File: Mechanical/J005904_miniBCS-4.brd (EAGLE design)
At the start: 146.1 x 146.1 mm, 173 parts, among them IC1 WIZ850io, J11 QWIIC_RIGHT_ANGLE, J14 A0/A1, J2 1734035-2, M2 TEENSY4.1, U1 ADA4084, U10 MAX11300GCM, U11 CAT811, U2 2G17, U3 ISL23425, U4 AD9833, U5 ISO1H815G, U6 78L12, U7 ADM3312/5, U8 2G17, U9 79L12, X1 OSC-OE-CFPS-9

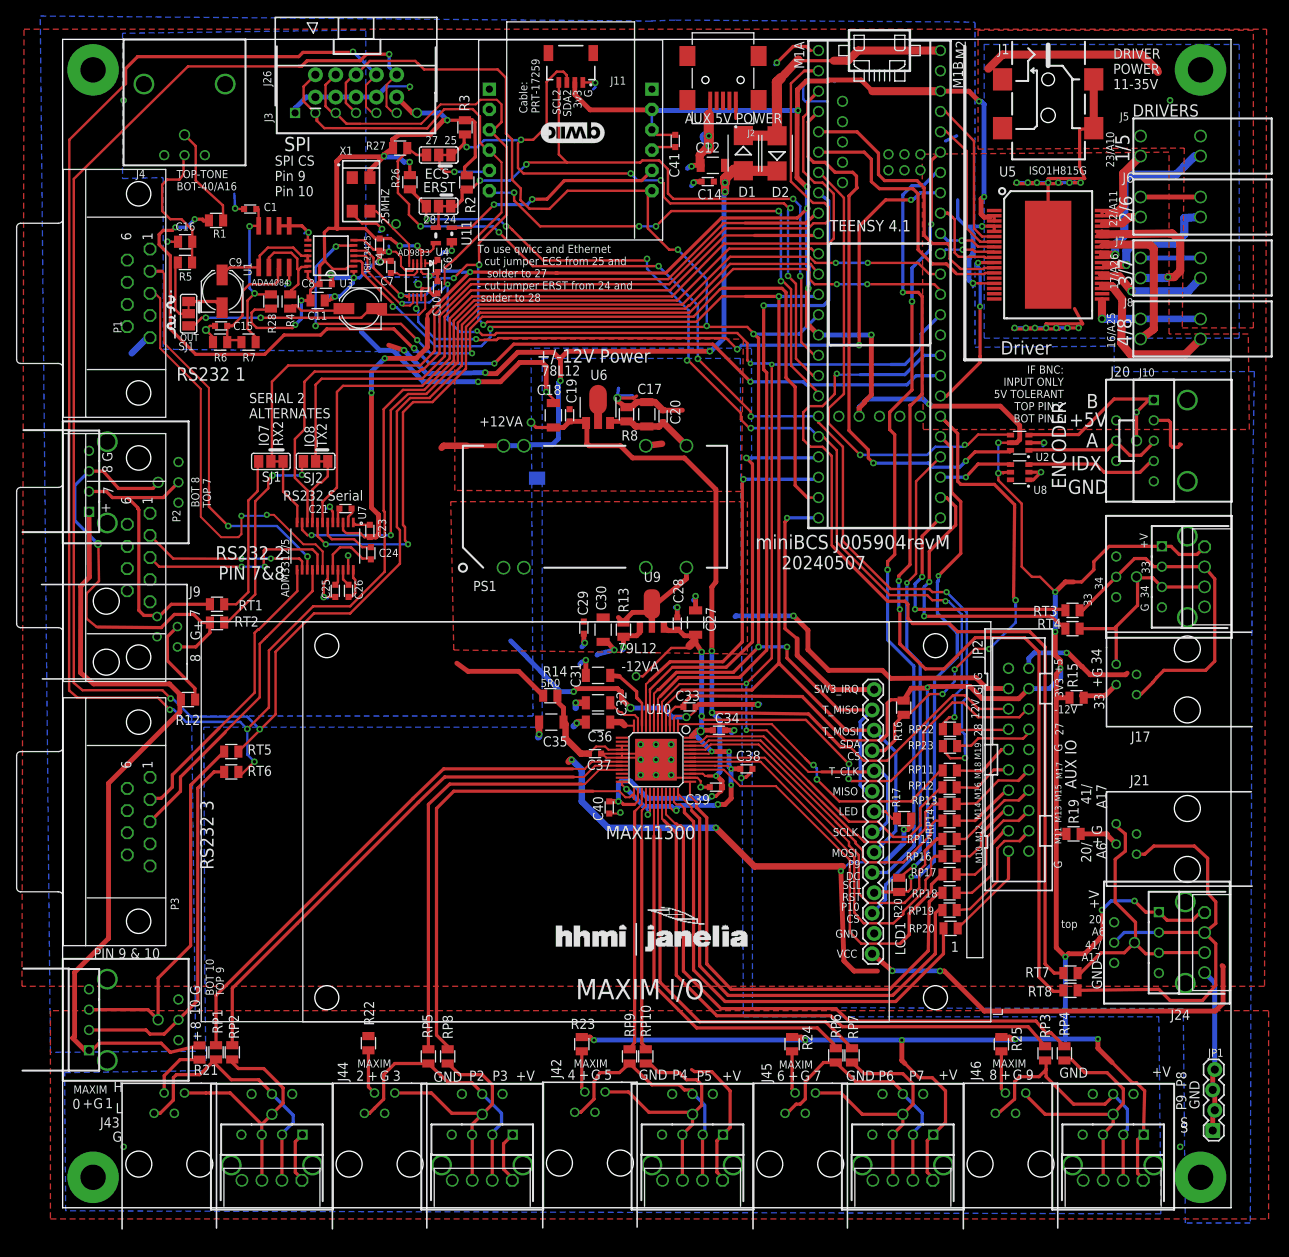
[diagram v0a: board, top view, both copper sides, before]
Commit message: Add SPI and I2C connectors
Add external connections for SPI with two chip selects on 10 pin ribbon or 7 pin header
Add QWIIC I2C connection
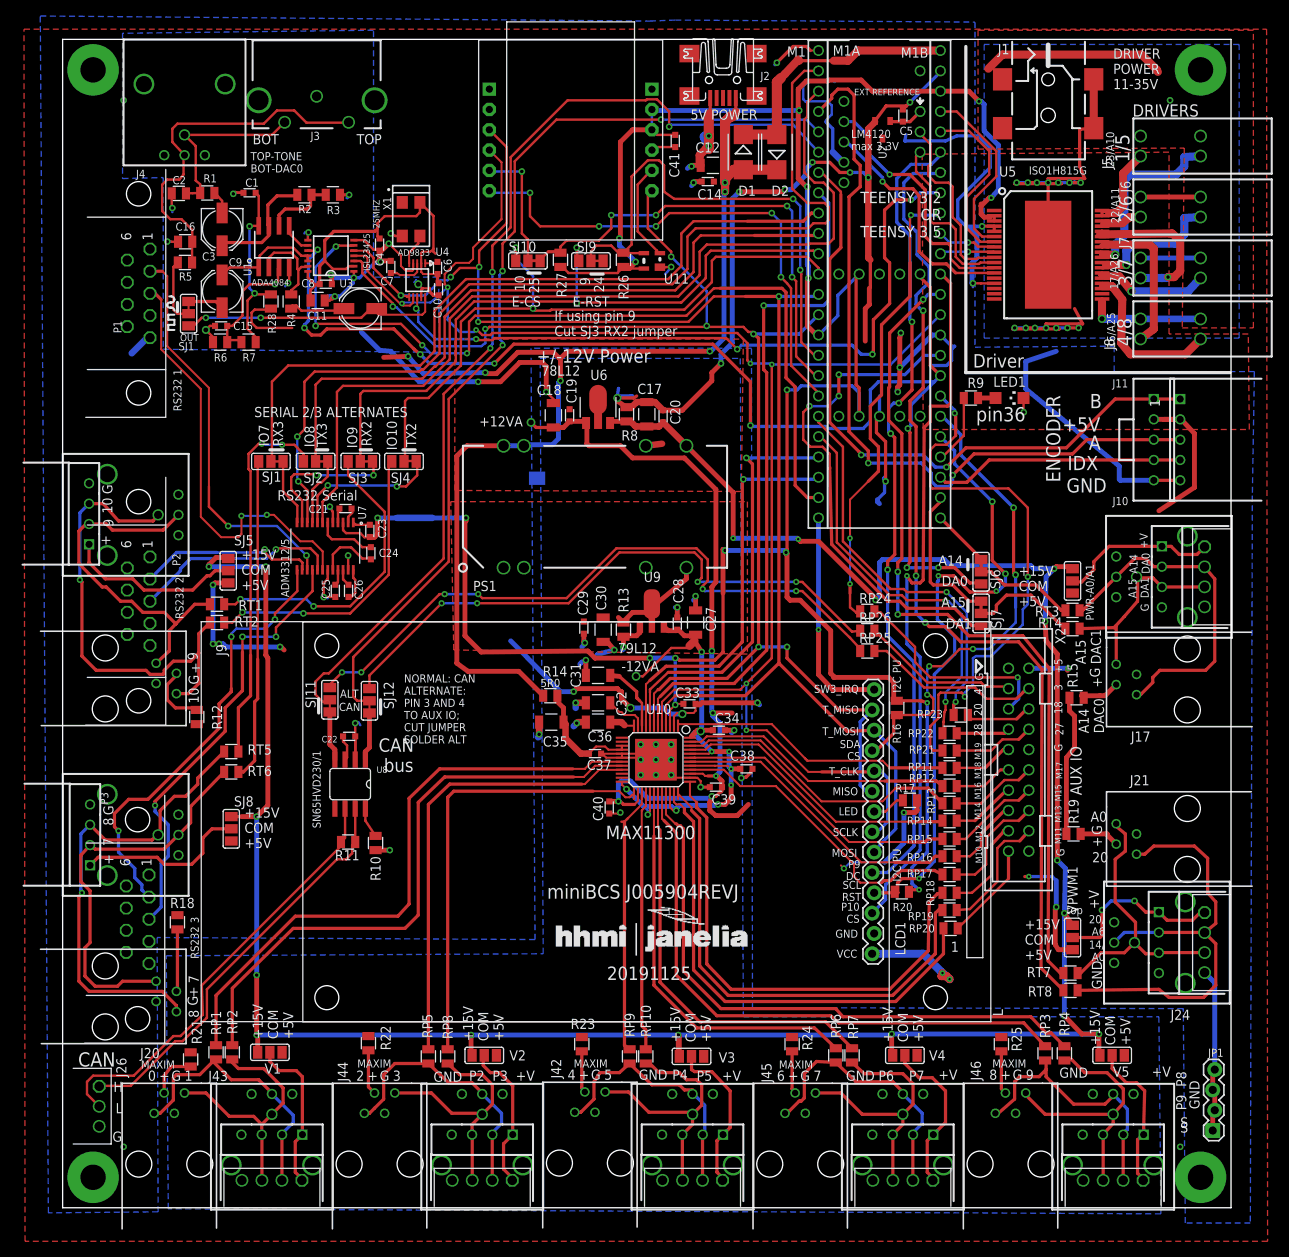
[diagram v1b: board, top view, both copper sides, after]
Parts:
- removed 25MHZ: (no value), STEVES_BU:PAD032
- removed ECS, ERST: (no value), jumper:SJ_2
- removed LOGO1: QWIIC_LOGO_8MM, SparkFun-Aesthetics:QWIIC_8MM
- removed M2: TEENSY4.1, teensy4.1.dist:TEENSY4.1
- added C2: 0.1, SteveS:0805S
- added C22, C5: .1uF, SteveS:0603S
- added C3: (no value), rcl:PANASONIC_C
- added LED1: (no value), adafruit:CHIPLED_1206
- added M1: TEENSY_3_5_2, Teensy_3_and_LC_Series_Boards_v1.4:TEENSY_3.X
- added PWR-A0/A1, SJ10, SJ11, SJ12, SJ3, SJ4, SJ5, SJ6, SJ7, SJ8, SJ9, V1, V2, V3, V4, V5, VPWM1: (no value), jumper:SJ_2
- added R10, R11, R18: 118, SteveS:0805S
- added R9, RP21, RP24, RP25, RP26: 100, SteveS:0805S
- IC1: value WIZ850io -> (none)
- J11: value QWIIC_RIGHT_ANGLE -> (none); device SparkFun-Connectors:JST04_1MM_RA -> STEVES_BU:103635-4
- J2: value 1734035-2 -> UX60-MB-5ST; device 1734035-2:CONN_1734035-2 -> STEVES_BU:UX60-MB-5ST
- J20: device STEVES_BU:DUAL-BNC -> STEVES_BU:0432024101
- J26: device STEVES_BU:2X5SHROUDED-RATH -> STEVES_BU:PHOENIX_1881451
- J3: value (none) -> RCA_DUAL; device STEVES_BU:AMPMODU7-RATH -> STEVES_BU:RCJ-22XX
- R2: device SteveS:0805S -> STEVES_BU:0805S
- R26, R27: value 4K99 -> 10K0
- R3: value 4K99 -> 10K0; device SteveS:0805S -> STEVES_BU:0805S
- U2: value 2G17 -> LM4120; device STEVES_BU:SOT23-6 -> texas:DBZ_R-PDSO-G3
- U8: value 2G17 -> SN65HVD230/1; device STEVES_BU:SOT23-6 -> Teaxs_Instruments:SO8
- moved J20 153.5 mm to (-2.67, 26.4), turned to 270 degrees
- moved J26 131.5 mm to (4.57, 12.7), turned to 270 degrees
- moved U8 92.3 mm to (35.9, 53.0), turned to 180 degrees
- moved J11 88.3 mm to (139.7, 96.0), turned to 270 degrees
- moved U2 42.7 mm to (102.5, 134.7), turned to 180 degrees
- moved R26 28.4 mm to (70.1, 118.5), turned to 90 degrees
- moved U11 26.2 mm to (73.7, 118.4)
- moved R27 24.4 mm to (62.2, 118.5), turned to 90 degrees
- moved J18 23.1 mm to (3.43, 46.6)
- moved J19 23.1 mm to (11.9, 46.6)
- moved R2 20.4 mm to (30.2, 126.6), turned to 180 degrees
- moved R3 18.5 mm to (33.8, 126.6), turned to 0 degrees
- moved P3 12.2 mm to (-0.13, 36.1)
- moved X1 6.97 mm to (43.6, 123.6)
- moved J9 5.84 mm to (-2.67, 66.2)
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- renumbered JP2 to X2
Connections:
- net +1V65A renamed +2V5A
- net +3V3ADDS renamed +5VADDS
- net DRV0 renamed N$30
- net DRV1 renamed N$32
- net DRV2 renamed N$40
- net DRV3 renamed N$17
- net DRV4 renamed N$10
- net DRV5 renamed N$14
- net DRV6 renamed N$2
- net DRV7 renamed N$18
- net ERST renamed N$52
- removed net !CS_TCH: LCD1.11, M2.38, R16.2
- removed net !TCHINT: LCD1.14, M2.32
- removed net !TFTRST: LCD1.4, M2.37, R20.2
- removed net A16: M2.40, R1.1
- removed net A17: M2.41, RT7.2
- removed net A6/20: M2.20/A6, RT8.2
- removed net CIPO: IC1.J2.6, J26.6, J3.4, LCD1.13, LCD1.9, M2.12/MISO, U10.7, U3.3
- removed net COPI: IC1.J1.3, J26.4, J3.3, LCD1.12, LCD1.6, M2.11/MOSI, U10.4, U3.5, U4.6
- removed net EA10: J18.3, J19.P$1, RT5.1
- removed net EA9: J18.2, J19.P$2, RT6.1
- removed net ENCA3V3: M2.2, U2.6
- removed net ENCB3V3: M2.5, U2.4
- removed net ETH_CS/SDA2: ECS.2, ECS.3, IC1.J1.5, J11.3, M2.25, R3.2
- removed net ETH_RST/SCL2: ERST.2, ERST.3, J11.4, M2.24, R2.2, U11.3
- removed net IDX3V3: M2.35, U8.4
- removed net PIN27/ALT_ECS: ECS.1, M2.27, R27.2, RP23.1
- removed net PIN28/ALT_ERST: ERST.1, M2.28, R26.2, RP22.1
- removed net PIN33: M2.33, RT3.2
- removed net PIN34: M2.34, RT4.2
- new net 0.1: C22.1, U8.3
- new net A0: M1.14/A0, RT7.2
- new net A14: M1.33/A14, RT3.2, SJ6.2, SJ6.3
- new net A15: M1.34/A15, RT4.2, SJ7.2, SJ7.3
- new net AREF: C5.1, M1.AREF, U2.1
- new net CANH: J26.1, R11.1, U8.7
- new net CANL: J26.2, R11.2, U8.6
- new net CANRX: M1.4, SJ11.2, SJ11.3, U8.4
- new net CANTX: M1.3, SJ12.2, SJ12.3, U8.1
- new net DAC0: M1.A14/DAC_32, M1.A21, SJ6.1, U3.10
- new net DAC1: M1.A22, SJ7.1
- new net EA8: J12.2, J13.P$2, J9.1, RT1.1
- new net EB7: J18.3, J19.P$1, J20.4, RT5.1
- new net ETH_CS: IC1.J1.5, M1.25, R27.2, SJ10.2, SJ10.3
- new net ETH_RST: M1.24, R26.2, SJ9.2, SJ9.3, U11.3
- new net MISO: IC1.J2.6, LCD1.13, LCD1.9, M1.12, U10.7, U3.3
- new net MOSI: IC1.J1.3, LCD1.12, LCD1.6, M1.11, U10.4, U3.5, U4.6
- new net N$19: LED1.A, R9.1
- new net N$39: R10.2, U8.8
- new net N$5: U1.5, U3.9
- new net N$6: M1.36/A17, R9.2
- new net N$61: RP21.2, X2.8
- new net N$63: RP23.2, X2.6
- new net N$64: RP24.2, X2.5
- new net N$65: RP25.2, X2.4
- new net N$66: RP26.2, X2.3
- new net N$7: R2.1, R3.1, U1.6
- new net PIN_18: M1.18/A4, RP24.1
- new net PIN_20: M1.20/A6, RT8.2
- new net PIN_27: M1.27, RP23.1
- new net PIN_28: M1.28, RP22.1
- new net PIN_3: RP26.1, SJ12.1
- new net PIN_39: M1.39/A20, RP21.1
- new net PIN_4: RP25.1, SJ11.1
- new net PWR7_8: J18.1, SJ8.2
- new net PWR9_10: J12.1, SJ5.2
- new net PWRA0_A1: J15.1, J16.1, PWR-A0/A1.2
- new net PWRPWM1_2: J23.1, J24.1, VPWM1.2
- new net PWR_P0-1: J33.1, J38.1, V1.2
- new net PWR_P2-3: J34.1, J39.1, V2.2
- new net PWR_P6-7: J36.1, J41.1, V4.2
- new net PWR_P8-9: J32.1, J37.1, V5.2
- new net SCL: LCD1.4, M1.37/A18, R20.2
- new net SDA: LCD1.11, M1.38/A19, R16.2
- new net SW1: LCD1.14, M1.32/A13
- new net VBAT: M1.VBAT
- new net VOUTB_1: C3.-, R1.1
- new net VUSB: M1.VUSB
- net !CS_DDS: now also M1.19/A5; no longer M2.19/A5/SCL
- net !CS_POT: now also M1.31/A12; no longer M2.31/A12
- net !MAXCNVT: now also M1.30; no longer M2.30
- net !MAXINT: now also M1.29; no longer M2.29
- net !MAX_CS: now also M1.6; no longer M2.6
- net !TFT_CS: now also M1.15/A1; no longer M2.36
- net +12VA: no longer X2.5
- net +15V: now also PWR-A0/A1.3, SJ5.3, SJ8.3, V1.3, V2.3, V3.3, V4.3, V5.3, VPWM1.3
- net +3V3D: now also M1.3.3V, M1.3.3V3, M1.3.3V4, M1.3.3V_32; no longer C10.1, C11.1, C4.1, C6.2, C8.2, J11.2, J12.1, J15.1, J16.1, J18.1, J23.1, J24.1, J26.9, J3.7, J32.1, J33.1, J34.1, J36.1, J37.1, J38.1, J39.1, J41.1, M2.3V3, M2.3V3_LO, M2.V33, R12.2, R15.1, R19.1, R2.1, R21.2, R22.2, R23.2, R24.2, R25.2, R28.2, R3.1, U2.5, U3.14, U3.2, U4.2, U8.5, X1.4, X2.4
- net +5VD: now also C10.1, C11.1, C4.1, C6.2, C8.2, J11.2, PWR-A0/A1.1, R12.2, R15.1, R18.2, R19.1, R21.2, R22.2, R23.2, R24.2, R25.2, R28.2, SJ5.1, SJ8.1, U3.14, U3.2, U4.2, V1.1, V2.1, V3.1, V4.1, V5.1, VPWM1.1, X1.4
- net -12VA: no longer X2.6
- net AGND: now also C2.2, C5.2, J3.1, M1.AGND, R3.2, U2.2; no longer U1.5, U1.6, X2.3
- net DAC0_OUT: now also C2.1, J3.2
- net DDS_OUT: now also J3.3
- net DGND: now also C22.2, J11.5, J20.3, LED1.C, M1.GND, M1.GND1, M1.GND3, M1.GND4, M1.GND6, M1.GND_32, R10.1; no longer J11.1, J20.P$3, J20.P$4, J26.1, J26.5, J26.7, J3.1, M2.AGND, M2.GND, M2.GND1, M2.GND2, U2.2, U8.1
- net EA7: now also J18.2, J19.P$2, J20.1, RT6.1; no longer J12.2, J13.P$2, J9.1, RT1.1
- net EN_A: now also J11.3, M1.2; no longer J20.P$2, U2.1
- net EN_B: now also J11.1, M1.5; no longer J20.P$1, U2.3
- net ETH_INT: now also M1.26; no longer M2.26
- net IDX: now also J11.4, M1.35/A16; no longer U8.3
- net N$1: now also J20.2, R18.1; no longer RP23.2, X2.8
- net N$13: no longer 25MHZ.P$1
- net N$37: now also C3.+, R2.2
- net PIN10: now also RT2.2, SJ4.3; no longer J26.10, J3.6, M2.10/CS, RT5.2
- net PIN7: now also RT6.2; no longer RT1.2
- net PIN8: now also RT5.2; no longer RT2.2
- net PIN9: now also RT1.2, SJ3.3; no longer J26.8, J3.5, M2.9, RT6.2
- net PWR_P4-5: now also V3.2
- net RX1: now also M1.0; no longer M2.0/RX
- net RX2: now also M1.9, SJ3.1, SJ3.2, SJ9.1, U7.11; no longer M2.7, SJ1.1, SJ1.2, U7.12
- net RX3: now also M1.7, SJ1.1, SJ1.2, U7.12; no longer M2.15/A1, U7.11
- net SCLK: now also M1.13; no longer J26.2, J3.2, M2.13/SCK
- net SOL1: now also M1.23/A9; no longer M2.23/A9
- net SOL2: now also M1.22/A8; no longer M2.22/A8
- net SOL3: now also M1.17/A3; no longer M2.17/A3
- net SOL4: now also M1.16/A2; no longer M2.16/A2
- net SOL5: now also M1.A10; no longer M2.18/A4/SDA
- net SOL6: now also M1.A11; no longer M2.39
- net SOL7: now also M1.A26; no longer M2.3
- net SOL8: now also M1.A25; no longer M2.4
- net TFT_DC: now also M1.21/A7; no longer M2.21/A7
- net TX1: now also M1.1; no longer M2.1/TX
- net TX2: now also M1.10, SJ10.1, SJ4.1, SJ4.2, U7.8; no longer M2.8, SJ2.1, SJ2.2, U7.9
- net TX3: now also M1.8, SJ2.1, SJ2.2, U7.9; no longer M2.14/A0, U7.8
- net VIN: now also M1.VIN; no longer M2.VIN
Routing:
- net +3V3D: track 803.7 -> 350.9 mm, vias 34 -> 17
- net +15V: track 11.3 -> 335.4 mm, vias 0 -> 17
- net CIPO: track 237.0 -> 0.00 mm, vias 7 -> 0
- net PIN9: track 267.6 -> 38.2 mm, vias 4 -> 2
- net PIN10: track 261.3 -> 37.5 mm, vias 3 -> 2
- net COPI: track 223.6 -> 0.00 mm, vias 5 -> 0
- net MOSI: track 0.00 -> 190.6 mm, vias 0 -> 5
- net MISO: track 0.00 -> 176.2 mm, vias 0 -> 7
- net DAC0: track 0.00 -> 156.0 mm, vias 0 -> 8
- net PIN27/ALT_ECS: track 136.7 -> 0.00 mm, vias 7 -> 0
- net CANRX: track 0.00 -> 133.2 mm, vias 0 -> 3
- net A6/20: track 130.9 -> 0.00 mm, vias 3 -> 0
- net CANTX: track 0.00 -> 126.2 mm, vias 0 -> 3
- net A16: track 124.0 -> 0.00 mm, vias 5 -> 0
- net PIN_20: track 0.00 -> 123.9 mm, vias 0 -> 3
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- removed copper zone on layer 1, net +3V3D
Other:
- board text added: "+15V COM +5V"
- board text added: "14/ A0"
- board text added: "18"
- board text added: "20"
- board text added: "20191125"
- board text added: "25MHZ"
- board text added: "33 34"
- board text added: "5V POWER"
- board text added: "A0"
- board text added: "A14"
- board text added: "A14 DA0"
- board text added: "A14 DAC0"
- board text added: "A15"
- board text added: "A15 DA1"
- board text added: "A15 DAC1"
- board text added: "A6-20 A17-41"
- board text added: "ALT"
- board text added: "AUX POWER"
- board text added: "CAN"
- board text added: "CAN bus"
- board text added: "DA0"
- board text added: "DA1"
- board text added: "DRIVER 11-35V"
- board text added: "DRIVERS 4 3 2 1 8 7 6 5"
- board text added: "E-CS"
- board text added: "E-RST"
- board text added: "ENCODER OR 2 & 5 IN"
- board text added: "ETHERNET"
- board text added: "EXT REFERENCE"
- board text added: "I2C PU"
- board text added: "IO10"
- board text added: "IO9"
- board text added: "If using pin 9 Cut SJ3 RX2 jumper"
- board text added: "LM4120 max 3.3V"
- board text added: "MAX 0 1"
- board text added: "MAX 2/3"
- board text added: "MAX 4/5"
- board text added: "MAX 6/7"
- board text added: "MAX 8/9"
- board text added: "NORMAL: CAN ALTERNATE: PIN 3 AND 4 TO AUX IO; CUT JUMPER SOLDER ALT"
- board text added: "PIN 9 PIN 10"
- board text added: "QWIIC"
- board text added: "REV M"
- board text added: "RX3"
- board text added: "SERIAL 1"
- board text added: "SERIAL 2 OR PINS 7 & 8"
- board text added: "SERIAL 2/3 ALTERNATES"
- board text added: "SERIAL 3"
- board text added: "SN65HVD230/1"
- board text added: "TEENSY 3.2 OR TEENSY 3.5"
- board text added: "TEENSY 4.1 USB/PWR"
- board text added: "TONE A16/40"
- board text added: "TOP-TONE BOT-DAC0"
- board text added: "TX3"
- board text added: "miniBCS J005904REVJ"
- board text added: "miniBCS-4"
- board text added: "pin36"
- board text removed: "-12V"
- board text removed: "12V"
- board text removed: "20240507"
- board text removed: "33"
- board text removed: "34"
- board text removed: "3V3"
- board text removed: "3v3"
- board text removed: "41/ A17"
- board text removed: "AUX 5V POWER"
- board text removed: "BOT 10"
- board text removed: "BOT 8"
- board text removed: "Cable: PRT-17259"
- board text removed: "IF BNC: INPUT ONLY 5V TOLERANT TOP PIN 2 BOT PIN 5"
- board text removed: "MAXIM I/O"
- board text removed: "PIN 9 & 10"
- board text removed: "RS232 2 PIN 7&8"
- board text removed: "SCL2"
- board text removed: "SDA2"
- board text removed: "SERIAL 2 ALTERNATES"
- board text removed: "SPI CS Pin 9 Pin 10"
- board text removed: "TEENSY 4.1"
- board text removed: "TOP 7"
- board text removed: "TOP 9"
- board text removed: "TOP-TONE BOT-40/A16"
- board text removed: "To use qwicc and Ethernet - cut jumper ECS from 25 and solder to 27 - cut jumper ERST from 24 and solder to 28"
- board text removed: "miniBCS J005904revM"
